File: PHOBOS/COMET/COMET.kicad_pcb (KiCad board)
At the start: 4 copper layers, 63.5 x 25.4 mm, 73 parts, among them J1 UART, J2 M/D, J5 Power/Arm, J6 USB_C_Receptacle_USB2.0_16P, Q1 SiSS63DN, Q2 BSD840N, Q3 SiSS63DN, SW1 SW_SPDT, SW3 KMR211GLFS, U1 MPL3115A2, U2 LSM6DS3, U3 W25Q128JVSIQ, U4 NCP1117-3.3_SOT223, U5 RP2040, Y1 ABM8-272-T3

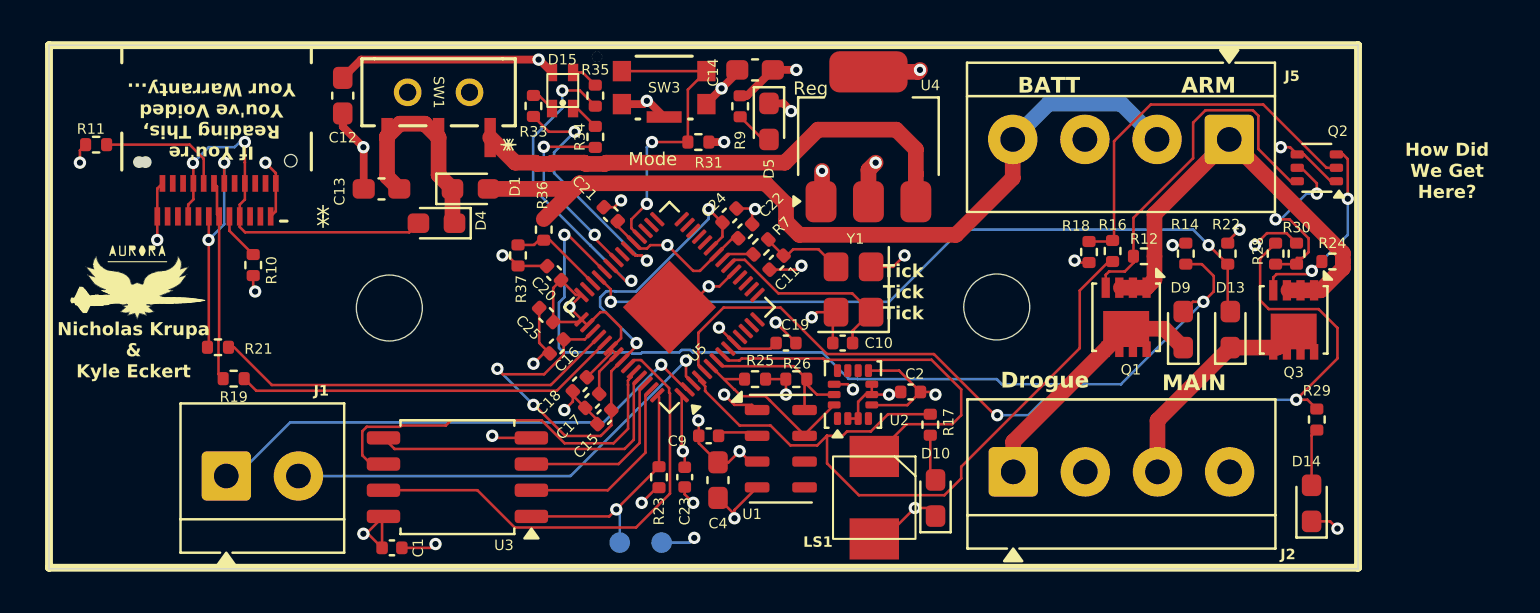
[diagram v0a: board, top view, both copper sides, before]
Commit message: USB updated, routed, added to BOM
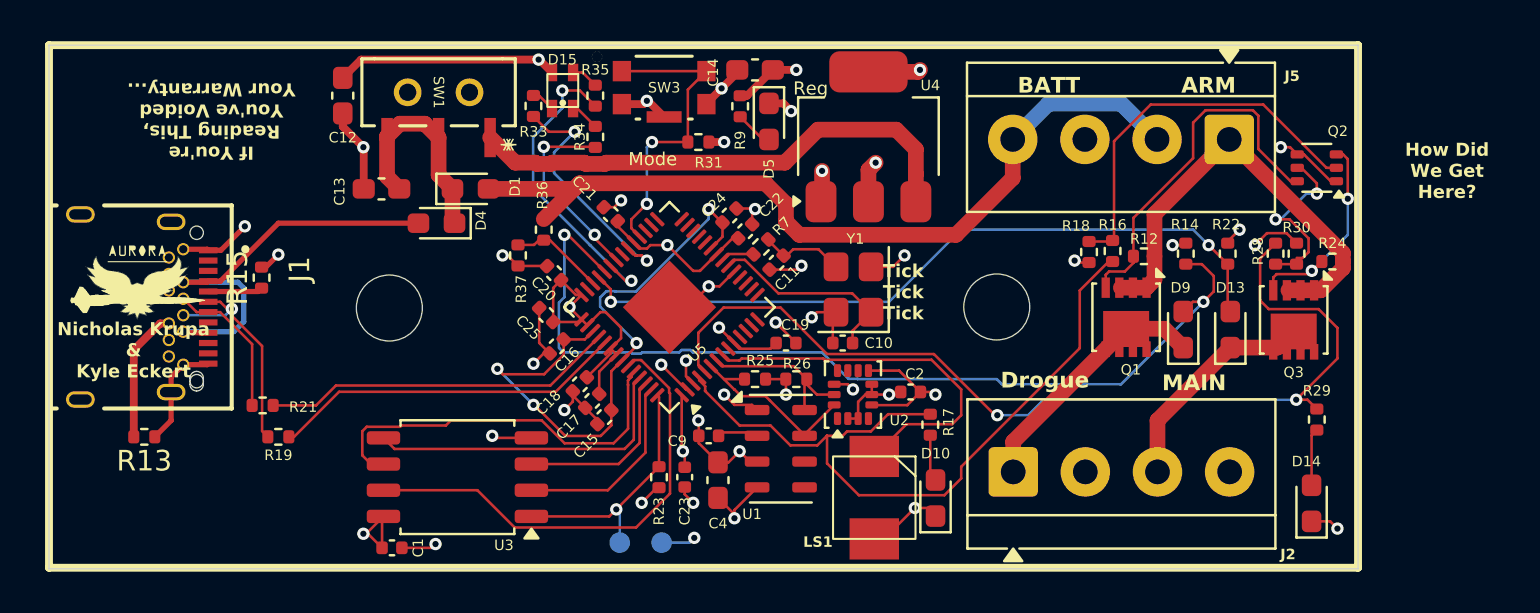
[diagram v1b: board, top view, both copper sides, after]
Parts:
- removed J6: USB_C_Receptacle_USB2.0_16P, External/Custom Parts:DX07S024JJ3R1300_JAE
- removed R10, R11: 5.1k, Resistor_SMD:R_0402_1005Metric
- added R13: 5.1k, Resistor_SMD:R_0402_1005Metric, F.Cu at (71.9, 79.9)
- added R15: 5.1k, Resistor_SMD:R_0402_1005Metric, F.Cu at (77.6, 72.1)
- J1: value UART -> USB4056-03-A_REVA2; footprint TerminalBlock_4Ucon:TerminalBlock_4Ucon_1x02_P3.50mm_Horizontal -> USB4056-03-A:GCT_USB4056-03-A_REVA2
- moved J1 10.8 mm to (68.8, 73.6), turned to -90 degrees
- moved R19 3.56 mm to (78.4, 79.9)
- moved R21 3.56 mm to (77.6, 78.3)
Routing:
- net /TX: track 25.1 -> 1.77 mm
- net /RX: track 22.4 -> 1.26 mm
- net Net-(J1-CC2): track 0.00 -> 6.45 mm
- net Net-(J6-CC2): track 6.19 -> 0.00 mm
- net /USB_D-: track 11.4 -> 7.22 mm, vias 2 -> 0
- net VBUS: track 18.8 -> 21.6 mm, vias 2 -> 0
- net Net-(J1-CC1): track 0.00 -> 2.66 mm
- net /USB_-: track 19.7 -> 17.2 mm
- net Net-(J6-CC1): track 2.33 -> 0.00 mm
- net GND: track 69.1 -> 71.4 mm, vias 31 -> 29
- net /USB_+: track 18.7 -> 17.2 mm
- net /USB_D+: track 9.68 -> 10.7 mm, vias 0 -> 1
